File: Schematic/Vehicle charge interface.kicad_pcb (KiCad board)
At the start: 2 copper layers, 20 parts, among them J1 Type 2 lock, J2 Stop charge switch, J3 Traction enable, J4 To Controllino, J5 Power in, K1 OMRON_P2R-05P

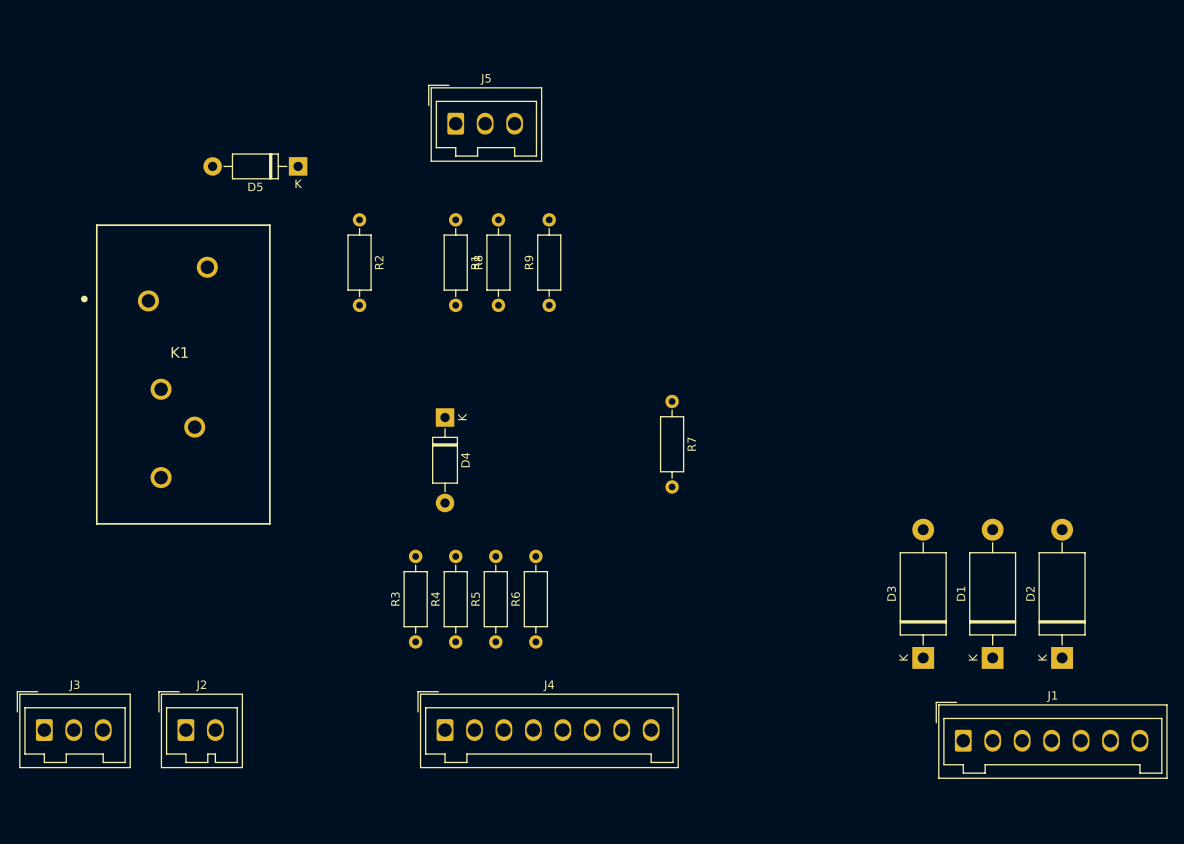
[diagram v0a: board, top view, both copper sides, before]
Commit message: Singlesided layout - upgraded to KiCad 6
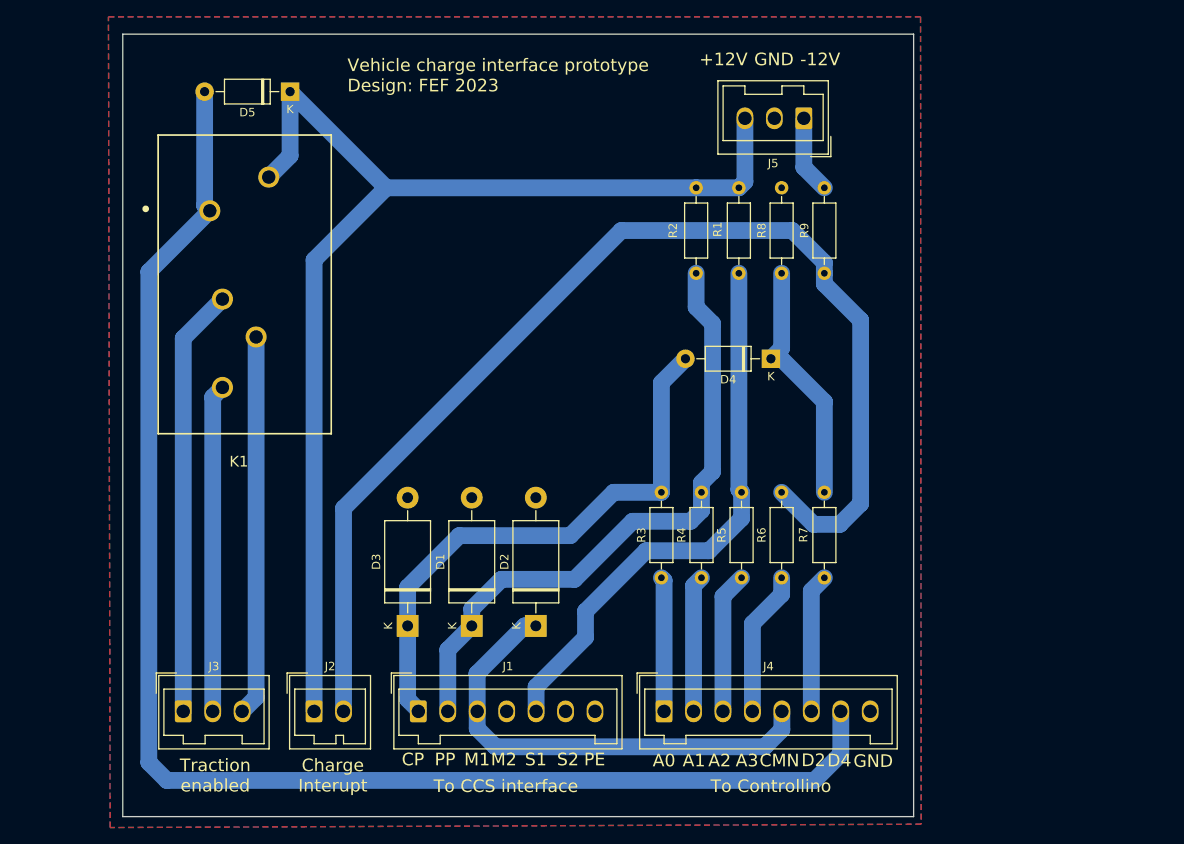
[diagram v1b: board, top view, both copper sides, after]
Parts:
- moved J1 64.9 mm to (151.1, 110.5)
- moved D2 62.7 mm to (165.1, 100.3)
- moved D1 62.0 mm to (157.5, 100.3)
- moved D3 61.4 mm to (149.9, 100.3)
- moved J5 41.4 mm to (196.9, 40.0), turned to 180 degrees
- moved R2 40.2 mm to (184.2, 48.3)
- moved D4 39.4 mm to (193.0, 68.6), turned to 180 degrees
- moved R1 33.9 mm to (189.2, 48.3)
- moved R8 33.9 mm to (194.3, 58.4)
- moved R9 32.9 mm to (199.4, 58.4)
- moved R3 30.2 mm to (180.0, 94.6)
- moved R4 30.2 mm to (184.8, 94.6)
- moved R5 30.2 mm to (189.5, 94.6)
- moved R6 30.2 mm to (194.3, 94.6)
- moved J4 26.1 mm to (180.3, 110.5)
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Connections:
- net /M1 renamed /CMN
- net Net-(D5-Pad2) renamed /D4
- net Net-(J4-Pad1) renamed /A0
- net Net-(J4-Pad2) renamed /A1
- net Net-(J4-Pad3) renamed /A2
- net Net-(J4-Pad4) renamed /A3
- net Net-(J4-Pad6) renamed /D2
- J5 pad 1: +12V -> -12V
- J5 pad 3: -12V -> +12V
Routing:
- net /D4: track 0.00 -> 172.5 mm
- net +12V: track 0.00 -> 143.6 mm
- net Net-(J2-Pad2): track 0.00 -> 139.0 mm
- net /PP: track 0.00 -> 75.1 mm
- net /CP: track 0.00 -> 67.2 mm
- net /S1: track 0.00 -> 66.7 mm
- net /CMN: track 0.00 -> 56.0 mm
- net Net-(J3-Pad1): track 0.00 -> 50.9 mm
- net Net-(J3-Pad3): track 0.00 -> 45.2 mm
- net Net-(J3-Pad2): track 0.00 -> 39.0 mm
- net Net-(D4-Pad1): track 0.00 -> 29.9 mm
- net /A3: track 0.00 -> 17.3 mm
- net /A2: track 0.00 -> 16.8 mm
- net /D2: track 0.00 -> 16.5 mm
- net /A1: track 0.00 -> 16.3 mm
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- added copper zone on B.Cu, net GND
- added copper zone on F.Cu, net GND
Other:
- board outline added: 94 x 93 mm
- net class Default removed
- board text added: "+12V"
- board text added: "-12V"
- board text added: "A0"
- board text added: "A1"
- board text added: "A2"
- board text added: "A3"
- board text added: "CMN"
- board text added: "CP"
- board text added: "Charge Interupt"
- board text added: "D2"
- board text added: "D4"
- board text added: "GND"
- board text added: "M1"
- board text added: "M2"
- board text added: "PE"
- board text added: "PP"
- board text added: "S1"
- board text added: "S2"
- board text added: "To CCS interface"
- board text added: "To Controllino"
- board text added: "Traction enabled"
- board text added: "Vehicle charge interface prototype Design: FEF 2023"
